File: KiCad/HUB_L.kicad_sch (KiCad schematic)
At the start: 51 parts, among them U5 GL850G-HHGXX(SSOP-28), Y4 12MHz

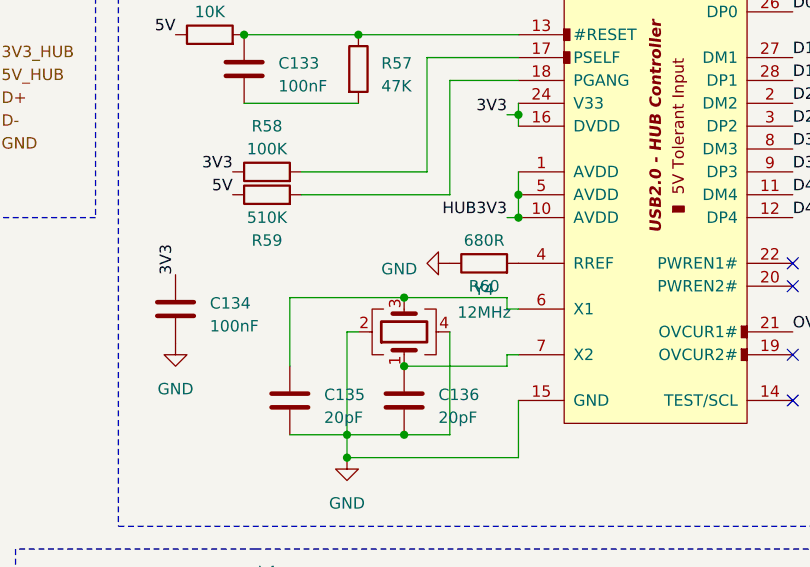
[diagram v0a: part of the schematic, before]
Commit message: Updated schematic
Added connections between hierarchical sheets, more code testing
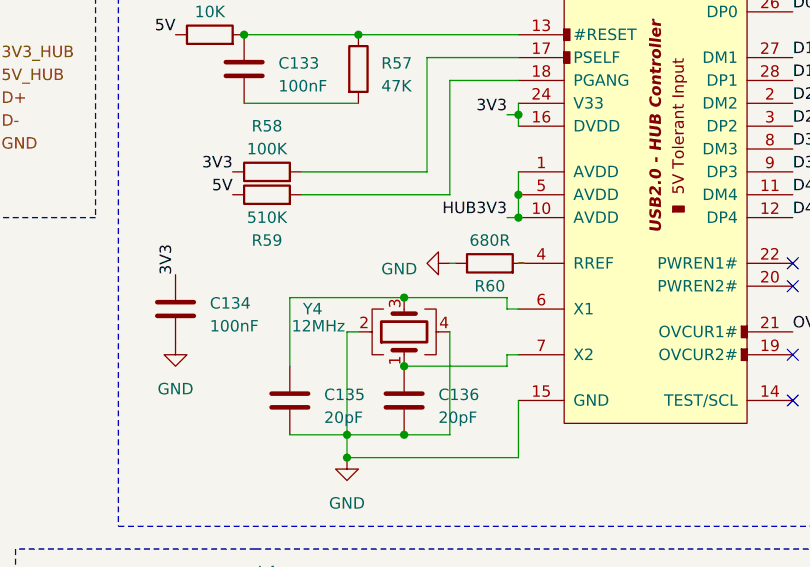
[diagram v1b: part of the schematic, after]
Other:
- moved on the sheet: R60
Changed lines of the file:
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@@
     (stroke (width 0) (type dash) (color 0 0 0 0))
+  )
+  (wire (pts (xy 227.965 64.77) (xy 227.33 64.77))
+    (stroke (width 0) (type default) (color 0 0 0 0))
   )
   (wire (pts (xy 77.47 143.51) (xy 83.82 143.51))
@@
   (wire (pts (xy 49.53 43.18) (xy 50.8 43.18))
     (stroke (width 0) (type solid) (color 0 0 0 0))
+  )
+  (wire (pts (xy 220.345 64.77) (xy 219.71 64.77))
+    (stroke (width 0) (type default) (color 0 0 0 0))
   )
   (polyline (pts (xy 22.86 182.88) (xy 22.86 20.32))
@@
     (pin "2")
   )
-  (symbol (lib_id "Device:R") (at 223.52 64.77 90) (unit 1)
+  (symbol (lib_id "Device:R") (at 224.155 64.77 90) (unit 1)
     (in_bom yes) (on_board yes)
-    (property "Reference" "R60" (id 0) (at 223.52 67.31 90))
-    (property "Value" "680R" (id 1) (at 223.52 62.23 90))
-    (property "Footprint" "Resistor_SMD:R_0603_1608Metric" (id 2) (at 223.52 66.548 90)
-      (effects (font (size 1.27 1.27)) hide)
-    )
-    (property "Datasheet" "~" (id 3) (at 223.52 64.77 0)
+    (property "Reference" "R60" (id 0) (at 224.155 67.31 90))
+    (property "Value" "680R" (id 1) (at 224.155 62.23 90))
+    (property "Footprint" "Resistor_SMD:R_0603_1608Metric" (id 2) (at 224.155 66.548 90)
+      (effects (font (size 1.27 1.27)) hide)
+    )
+    (property "Datasheet" "~" (id 3) (at 224.155 64.77 0)
       (effects (font (size 1.27 1.27)) hide)
     )
@@
   )
   (symbol (lib_id "Device:Crystal_GND24") (at 214.63 72.39 90) (unit 1)
-    (in_bom yes) (on_board yes) (fields_autoplaced)
-    (property "Reference" "Y4" (id 0) (at 223.52 67.691 90))
-    (property "Value" "12MHz" (id 1) (at 223.52 70.231 90))
+    (in_bom yes) (on_board yes)
+    (property "Reference" "Y4" (id 0) (at 204.47 69.85 90))
+    (property "Value" "12MHz" (id 1) (at 205.105 71.755 90))
     (property "Footprint" "Crystal:Crystal_SMD_3225-4Pin_3.2x2.5mm" (id 2) (at 214.63 72.39 0)
       (effects (font (size 1.27 1.27)) hide)
